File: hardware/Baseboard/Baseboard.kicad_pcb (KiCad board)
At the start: 2 copper layers, 160 x 160 mm, 77 parts, among them IC1 74HC00, IC10 W65C22, IC11 74HC148, IC12 74HC273, IC2 W65C02, IC3 74HC138, IC4 SYSTEM ROM, IC5 RAM, IC6 W65C22, IC7 W65C51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

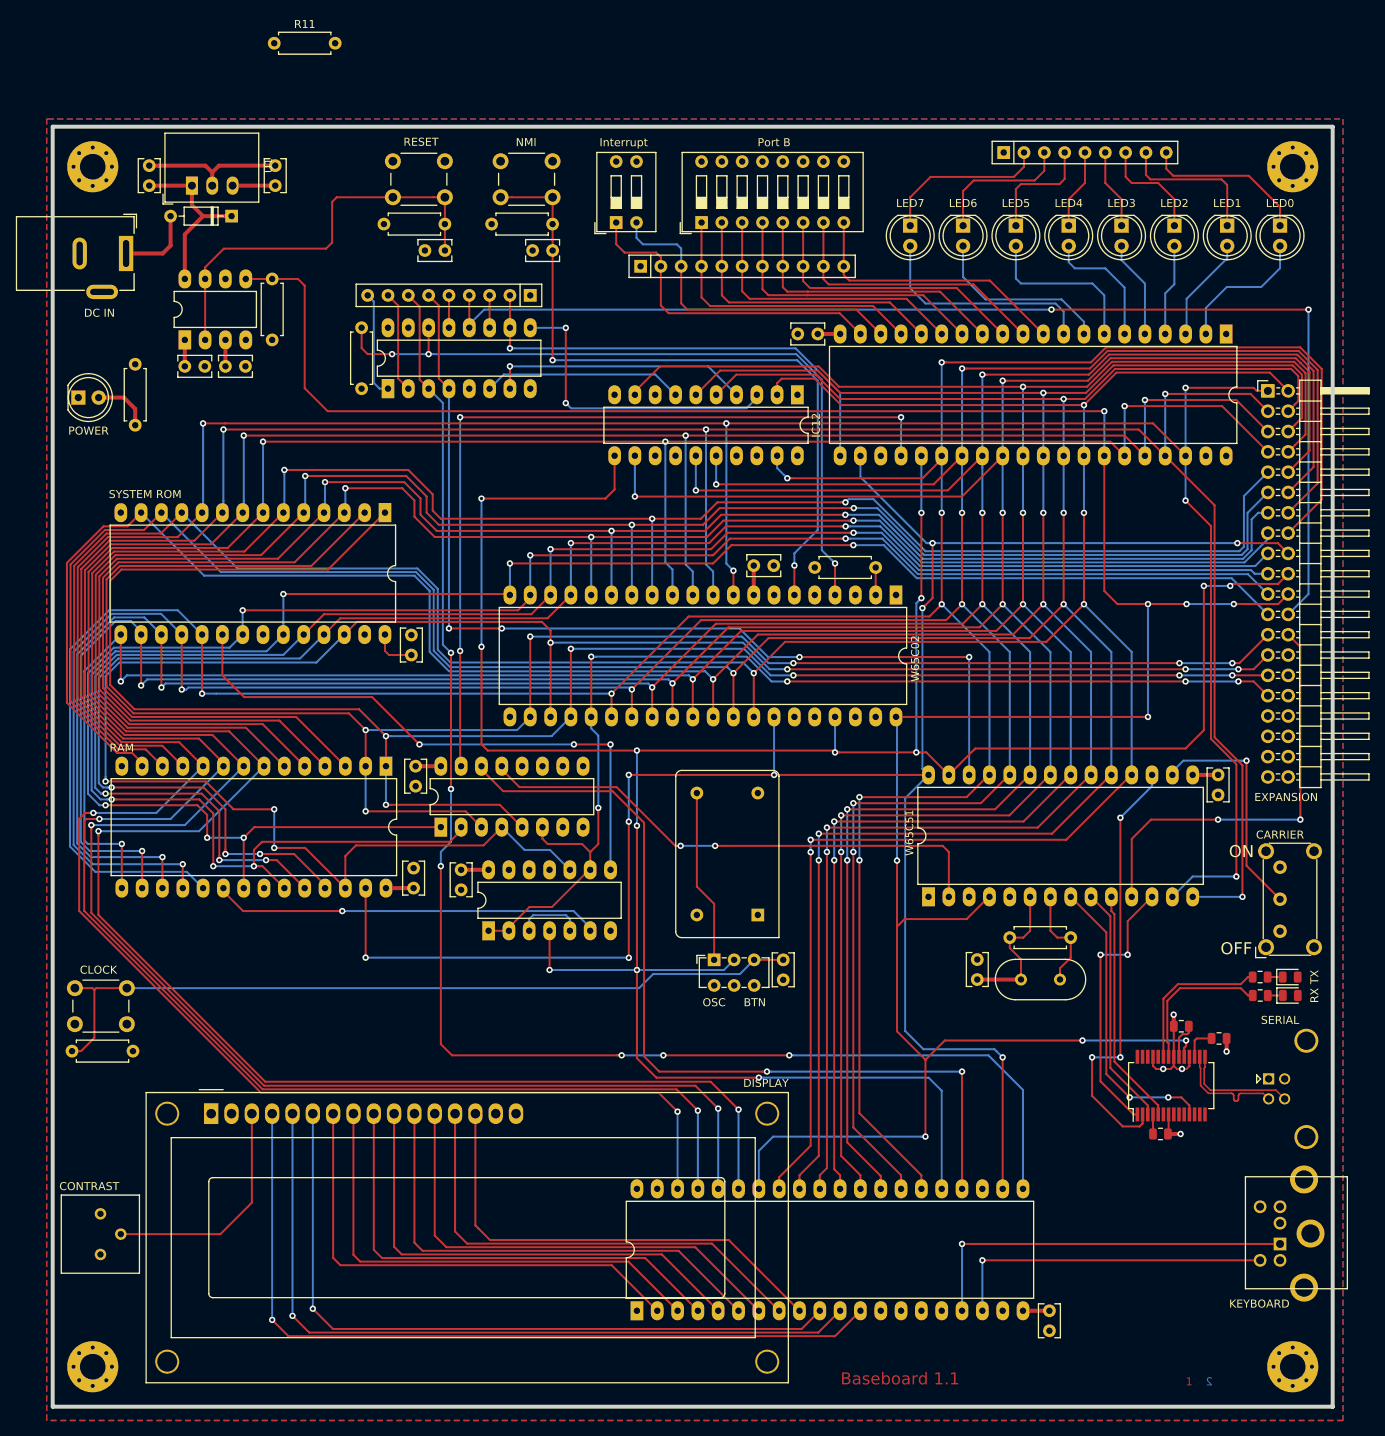
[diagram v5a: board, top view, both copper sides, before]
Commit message: Optimize routing, add RDY and SYNC to expansion header
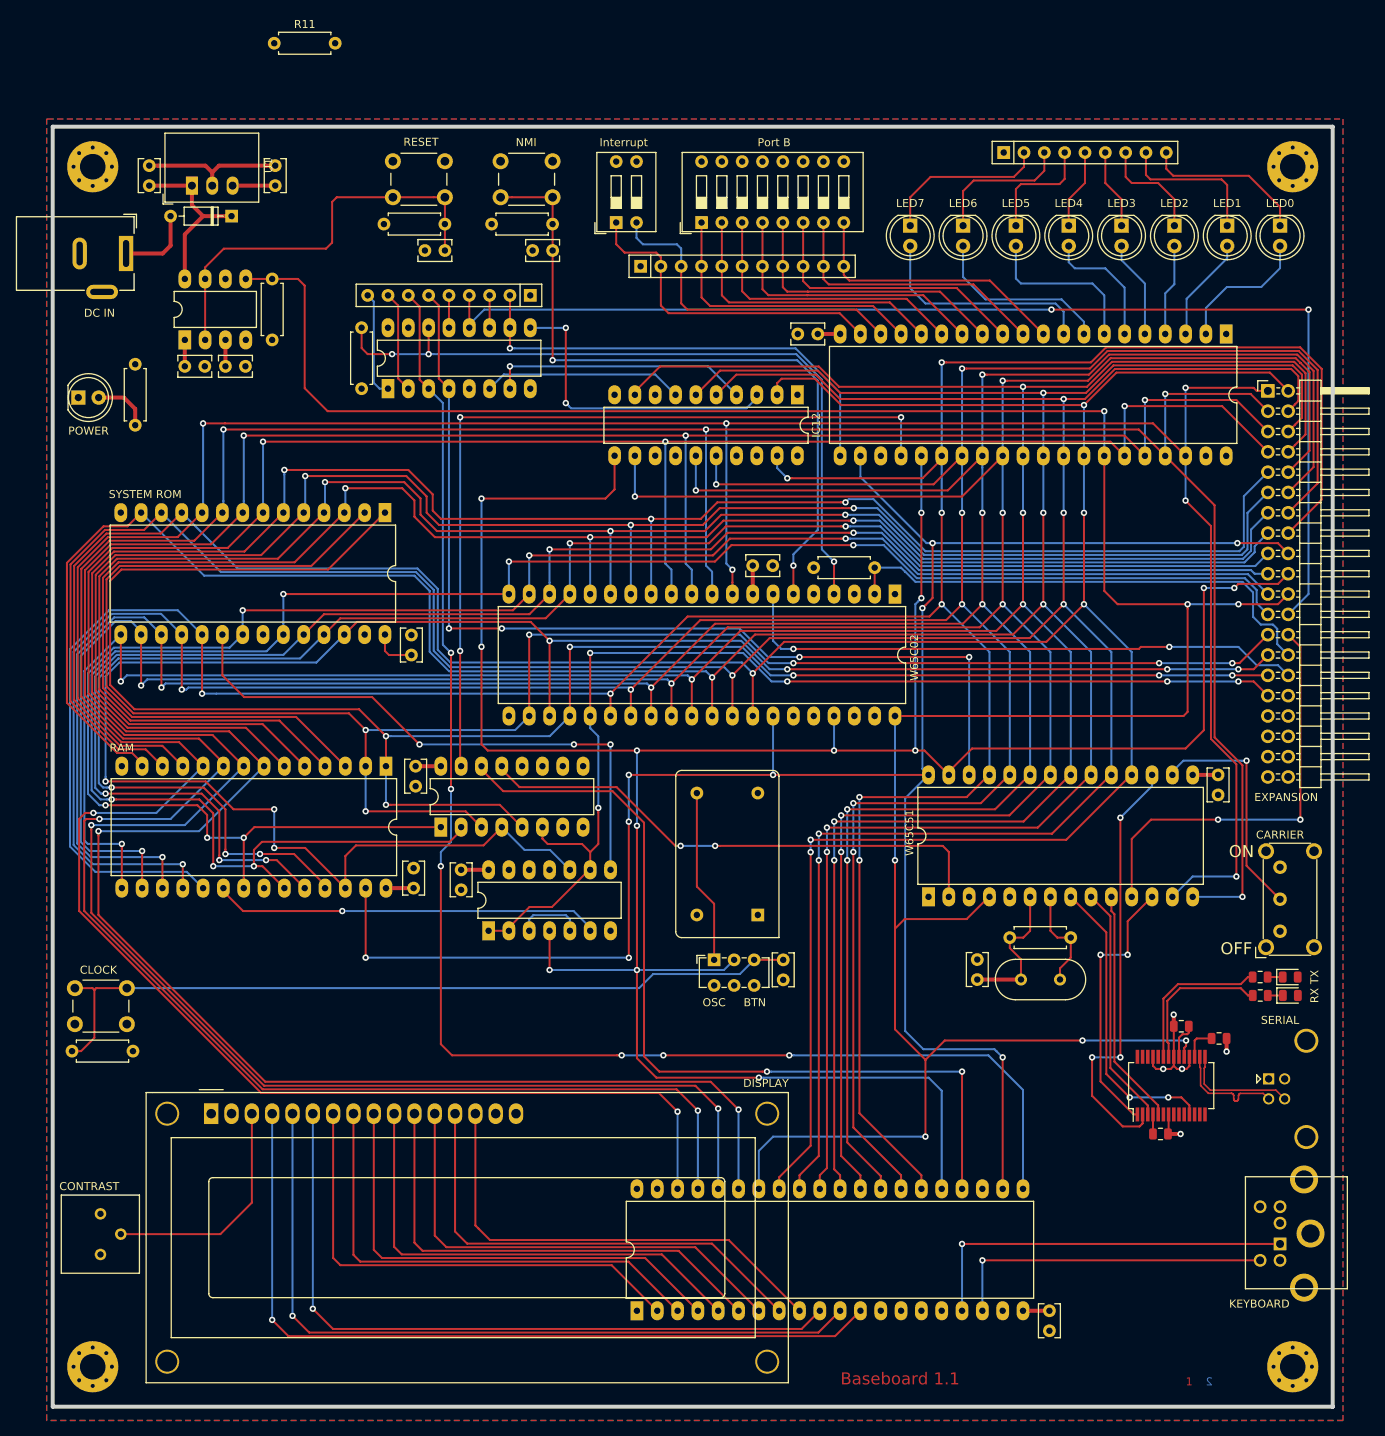
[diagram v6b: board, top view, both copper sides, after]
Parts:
- moved IC2 0.17 mm to (243.3, 109.7)
- moved R3 0.13 mm to (233.2, 106.4)
- moved C2 0.13 mm to (225.6, 106.2)
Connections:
- IC10 pad 13: Net-(IC10-Pad13) -> (no net)
- IC10 pad 14: Net-(IC10-Pad14) -> (no net)
- IC10 pad 15: Net-(IC10-Pad15) -> (no net)
- IC10 pad 16: Net-(IC10-Pad16) -> (no net)
- IC10 pad 19: Net-(IC10-Pad19) -> (no net)
- IC10 pad 39: Net-(IC10-Pad39) -> (no net)
- IC10 pad 40: Net-(IC10-Pad40) -> (no net)
- IC11 pad 15: Net-(IC11-Pad15) -> (no net)
- IC12 pad 1: /IRQ/~IRQ_Read -> Net-(IC12-Pad1)
- IC12 pad 13: Net-(IC12-Pad13) -> (no net)
- IC12 pad 14: Net-(IC12-Pad14) -> (no net)
- IC12 pad 17: Net-(IC12-Pad17) -> (no net)
- IC12 pad 18: Net-(IC12-Pad18) -> (no net)
- IC12 pad 8: Net-(IC12-Pad8) -> (no net)
- IC2 pad 1: /IRQ/~IRQ_Read -> (no net)
- IC2 pad 2: Net-(IC2-Pad2) -> /IO/RDY
- IC2 pad 3: Net-(IC2-Pad3) -> (no net)
- IC2 pad 35: Net-(IC2-Pad35) -> (no net)
- IC2 pad 39: Net-(IC2-Pad39) -> (no net)
- IC2 pad 5: Net-(IC2-Pad5) -> (no net)
- IC2 pad 7: Net-(IC2-Pad7) -> /IO/Sync
- IC3 pad 10: Net-(IC3-Pad10) -> (no net)
- IC3 pad 11: Net-(IC3-Pad11) -> (no net)
- IC3 pad 12: Net-(IC3-Pad12) -> (no net)
- IC3 pad 7: Net-(IC3-Pad7) -> (no net)
- IC3 pad 9: Net-(IC3-Pad9) -> (no net)
- IC6 pad 39: Net-(IC6-Pad39) -> (no net)
- IC6 pad 40: Net-(IC6-Pad40) -> (no net)
- IC7 pad 5: Net-(IC7-Pad5) -> (no net)
- IC8 pad 6: Net-(IC8-Pad6) -> (no net)
- IC9 pad 10: Net-(IC9-Pad10) -> (no net)
- IC9 pad 12: Net-(IC9-Pad12) -> (no net)
- IC9 pad 13: Net-(IC9-Pad13) -> (no net)
- IC9 pad 14: Net-(IC9-Pad14) -> (no net)
- IC9 pad 26: Net-(IC9-Pad26) -> (no net)
- IC9 pad 27: Net-(IC9-Pad27) -> (no net)
- IC9 pad 28: Net-(IC9-Pad28) -> (no net)
- IC9 pad 6: Net-(IC9-Pad6) -> (no net)
- IC9 pad 9: Net-(IC9-Pad9) -> (no net)
- R11 pad 1: /IRQ/~IRQ_Read -> Net-(IC12-Pad1)
- R3 pad 2: Net-(IC2-Pad2) -> /IO/RDY
- RV1 pad 3: Net-(RV1-Pad3) -> (no net)
- X2 pad 1: Net-(X2-Pad1) -> (no net)
- X3 pad 28: Net-(X3-Pad28) -> /IO/RDY
- X3 pad 30: Net-(X3-Pad30) -> /IO/Sync
- X3 pad 32: Net-(X3-Pad32) -> (no net)
- X3 pad 33: Net-(X3-Pad33) -> (no net)
- X3 pad 34: Net-(X3-Pad34) -> (no net)
- X3 pad 35: Net-(X3-Pad35) -> (no net)
- X3 pad 36: Net-(X3-Pad36) -> (no net)
- X3 pad 37: Net-(X3-Pad37) -> (no net)
- X3 pad 38: Net-(X3-Pad38) -> (no net)
- X4 pad 2: Net-(X4-Pad2) -> (no net)
- X4 pad 6: Net-(X4-Pad6) -> (no net)
- XTAL1 pad 1: Net-(XTAL1-Pad1) -> (no net)
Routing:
- net /IO/Sync: track 0.00 -> 72.2 mm, vias 0 -> 2
- net /IO/RDY: track 0.00 -> 62.4 mm
- net /IO/~Reset: track 342.0 -> 348.5 mm, vias 9 -> 7
- net Net-(IC2-Pad2): track 3.44 -> 0.00 mm
- net /IO/A11: track 239.6 -> 240.6 mm
- net /IO/A15: track 138.5 -> 139.3 mm
- net /IO/A6: track 218.8 -> 218.0 mm
- net /IO/A13: track 248.7 -> 247.9 mm
- net /IO/A3: track 364.5 -> 363.9 mm

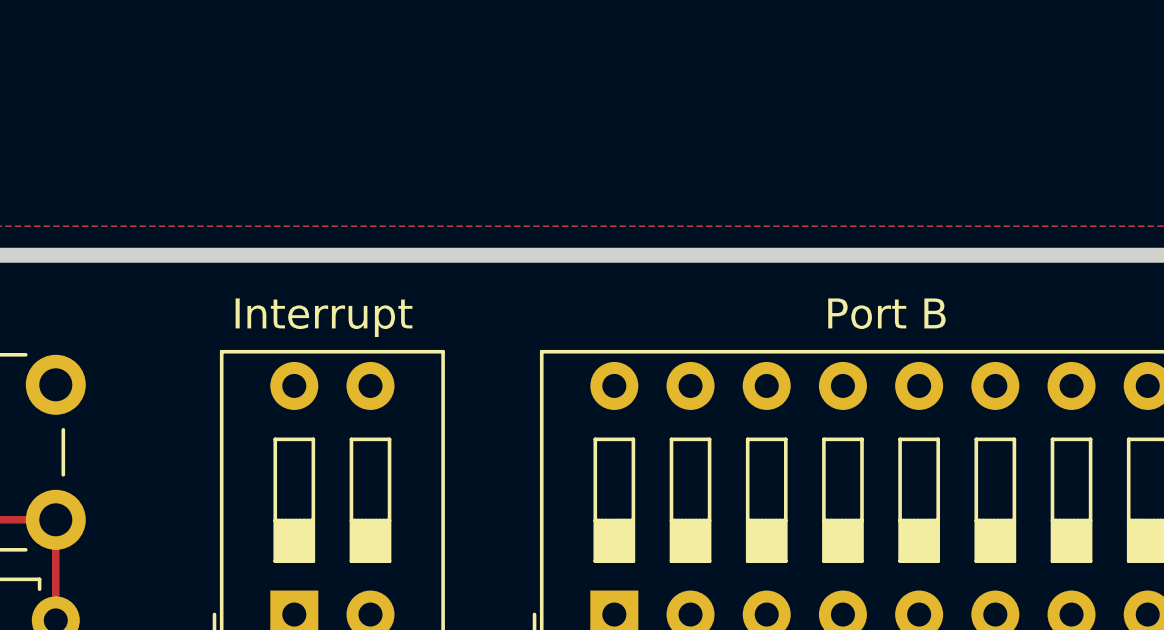
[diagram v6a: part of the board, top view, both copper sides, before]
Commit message: Rename PortB and the interrupt DIP switch
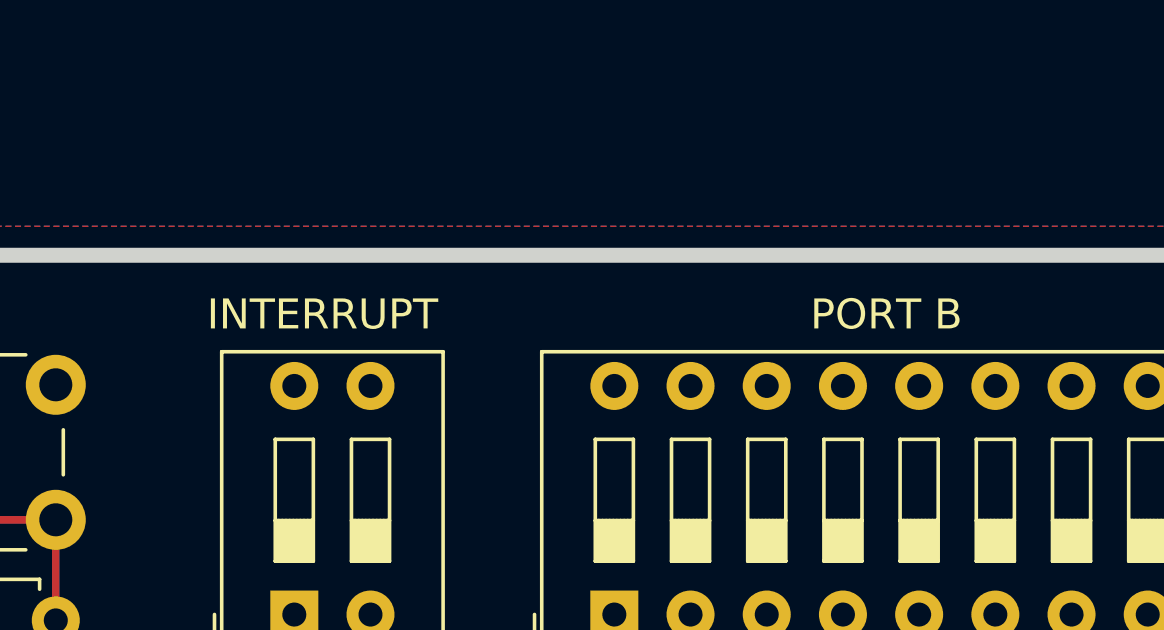
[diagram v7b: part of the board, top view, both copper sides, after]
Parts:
- SW2: value Interrupt -> INTERRUPT
- SW3: value Port B -> PORT B
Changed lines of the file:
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@@
     (add_net "Net-(IC1-Pad6)")
     (add_net "Net-(IC1-Pad8)")
+    (add_net "Net-(IC10-Pad13)")
+    (add_net "Net-(IC10-Pad14)")
+    (add_net "Net-(IC10-Pad15)")
+    (add_net "Net-(IC10-Pad16)")
+    (add_net "Net-(IC10-Pad19)")
+    (add_net "Net-(IC10-Pad39)")
+    (add_net "Net-(IC10-Pad40)")
     (add_net "Net-(IC11-Pad1)")
     (add_net "Net-(IC11-Pad11)")
     (add_net "Net-(IC11-Pad13)")
+    (add_net "Net-(IC11-Pad15)")
     (add_net "Net-(IC11-Pad2)")
     (add_net "Net-(IC11-Pad6)")
@@
     (add_net "Net-(IC11-Pad9)")
     (add_net "Net-(IC12-Pad1)")
+    (add_net "Net-(IC12-Pad13)")
+    (add_net "Net-(IC12-Pad14)")
+    (add_net "Net-(IC12-Pad17)")
+    (add_net "Net-(IC12-Pad18)")
+    (add_net "Net-(IC12-Pad8)")
+    (add_net "Net-(IC2-Pad1)")
+    (add_net "Net-(IC2-Pad3)")
+    (add_net "Net-(IC2-Pad35)")
+    (add_net "Net-(IC2-Pad39)")
+    (add_net "Net-(IC2-Pad5)")
+    (add_net "Net-(IC3-Pad10)")
+    (add_net "Net-(IC3-Pad11)")
+    (add_net "Net-(IC3-Pad12)")
+    (add_net "Net-(IC3-Pad7)")
+    (add_net "Net-(IC3-Pad9)")
+    (add_net "Net-(IC6-Pad39)")
+    (add_net "Net-(IC6-Pad40)")
+    (add_net "Net-(IC7-Pad5)")
     (add_net "Net-(IC7-Pad7)")
+    (add_net "Net-(IC8-Pad6)")
+    (add_net "Net-(IC9-Pad10)")
+    (add_net "Net-(IC9-Pad12)")
+    (add_net "Net-(IC9-Pad13)")
+    (add_net "Net-(IC9-Pad14)")
     (add_net "Net-(IC9-Pad22)")
     (add_net "Net-(IC9-Pad23)")
+    (add_net "Net-(IC9-Pad26)")
+    (add_net "Net-(IC9-Pad27)")
+    (add_net "Net-(IC9-Pad28)")
+    (add_net "Net-(IC9-Pad6)")
+    (add_net "Net-(IC9-Pad9)")
+    (add_net "Net-(RV1-Pad3)")
+    (add_net "Net-(X2-Pad1)")
+    (add_net "Net-(X3-Pad32)")
+    (add_net "Net-(X3-Pad33)")
+    (add_net "Net-(X3-Pad34)")
+    (add_net "Net-(X3-Pad35)")
+    (add_net "Net-(X3-Pad36)")
+    (add_net "Net-(X3-Pad37)")
+    (add_net "Net-(X3-Pad38)")
+    (add_net "Net-(X4-Pad2)")
+    (add_net "Net-(X4-Pad6)")
+    (add_net "Net-(XTAL1-Pad1)")
   )
   (net_class Power ""
@@
       (effects (font (size 1 1) (thickness 0.15)))
     )
-    (fp_text value "Port B" (at 10 9.068 180) (layer F.SilkS)
+    (fp_text value "PORT B" (at 10 9.068 180) (layer F.SilkS)
       (effects (font (size 1 1) (thickness 0.15)))
     )
@@
       (effects (font (size 1 1) (thickness 0.15)))
     )
-    (fp_text value Interrupt (at 10 0.94 180) (layer F.SilkS)
+    (fp_text value INTERRUPT (at 10 0.94 180) (layer F.SilkS)
       (effects (font (size 1 1) (thickness 0.15)))
     )
